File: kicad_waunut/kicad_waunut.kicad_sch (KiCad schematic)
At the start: 94 parts, among them J1 Conn_01x02_Pin, J2 Conn_01x06_Pin, Q1 NPN, Q2 NPN, Q3 NPN, Q4 NPN, Q5 NPN, Q6 NPN, Q7 NPN, Q8 NPN, U1 TSR1-2450E, U2 ATtiny861A-S

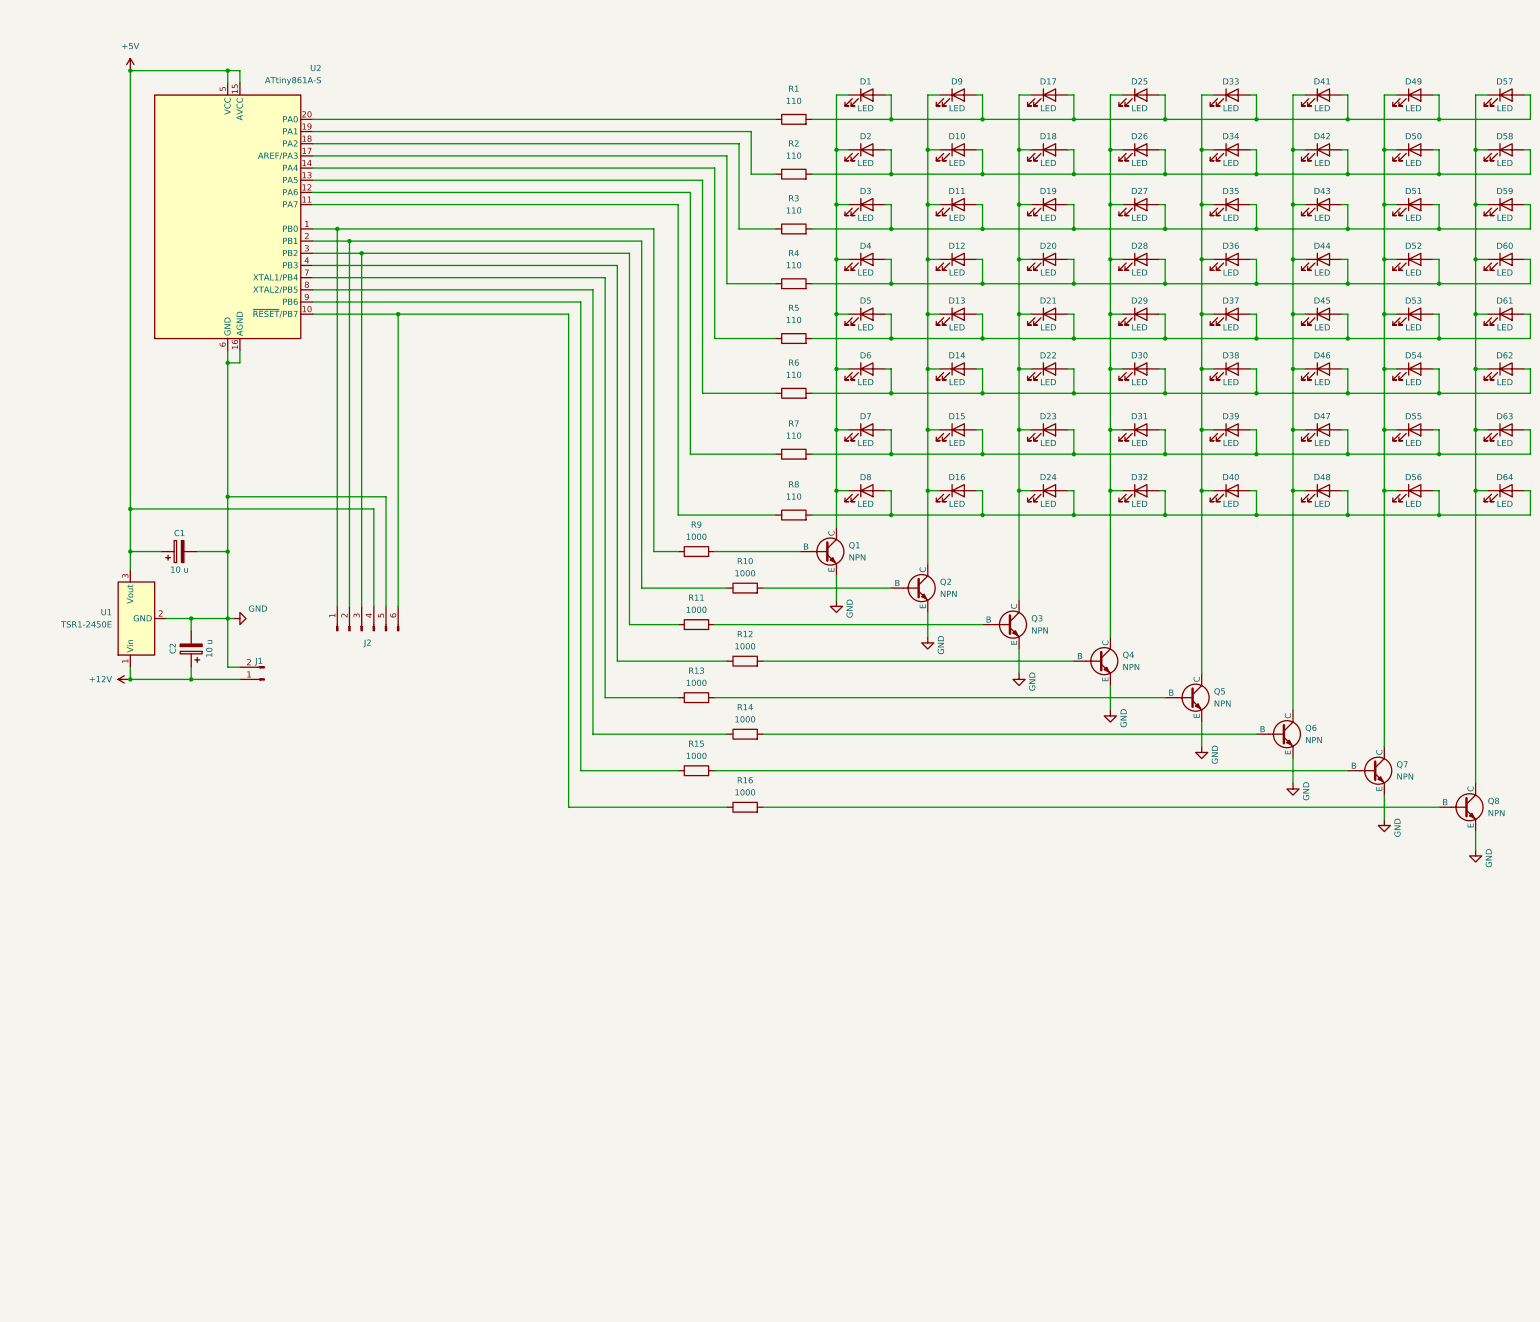
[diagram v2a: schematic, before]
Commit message: Kicad projekti tiedostoja siirrelty, selkä rev2 init ja waunujen skema muutosta.
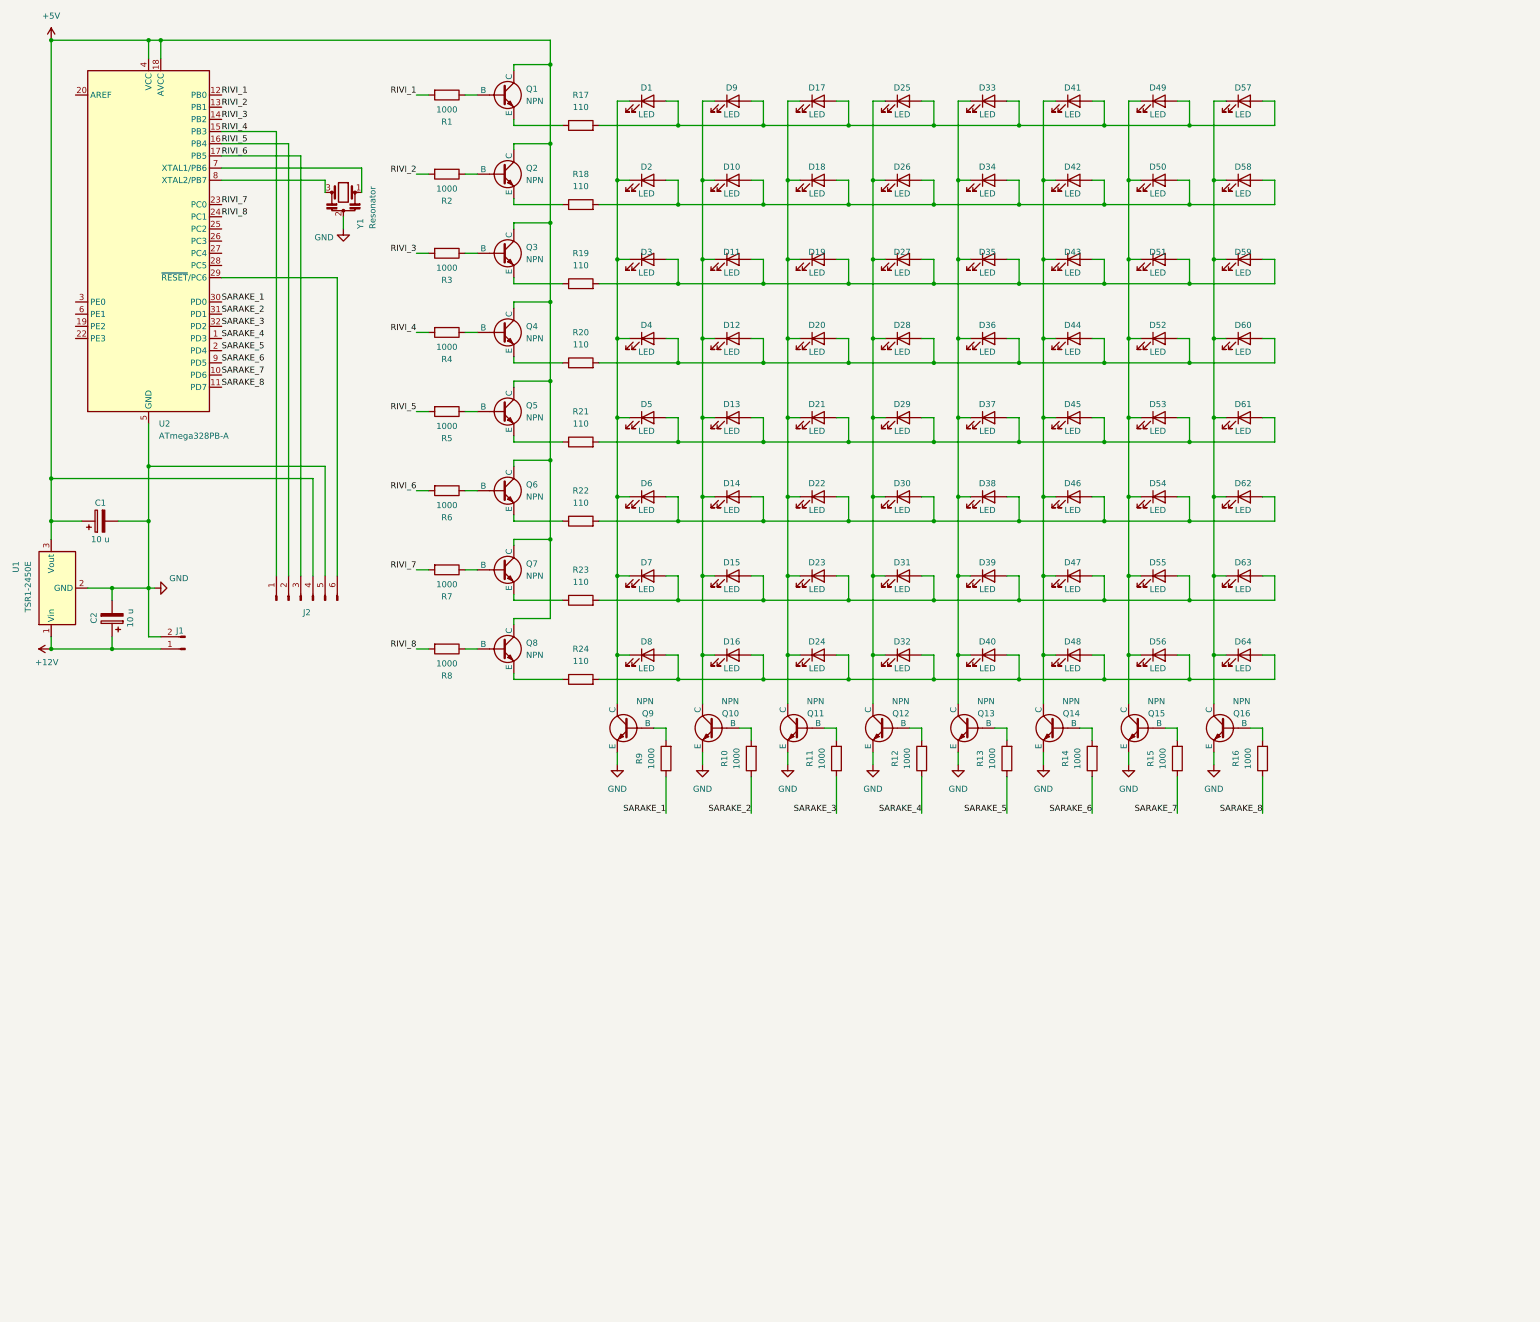
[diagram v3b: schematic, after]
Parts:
- removed U2: ATtiny861A-S, Package_SO:SOIC-20W_7.5x12.8mm_P1.27mm, symbol MCU_Microchip_ATtiny:ATtiny861A-S
- added Q10, Q11, Q12, Q13, Q14, Q15, Q16, Q9: NPN, Package_TO_SOT_SMD:SOT-23, symbol Simulation_SPICE:NPN
- added R1, R2, R3, R4, R5, R6, R7, R8: 1000, Resistor_SMD:R_1206_3216Metric_Pad1.30x1.75mm_HandSolder, symbol Device:R
- added U2: ATmega328PB-A, Package_QFP:TQFP-32_7x7mm_P0.8mm, symbol MCU_Microchip_ATmega:ATmega328PB-A
- added Y1: Resonator, symbol Device:Resonator
- renumbered R1 to R17, R2 to R18, R3 to R19, R4 to R20, R5 to R21, R6 to R22, R7 to R23, R8 to R24
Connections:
- net +5V: now also Q1.1 (C), Q2.1 (C), Q3.1 (C), Q4.1 (C), Q5.1 (C), Q6.1 (C), Q7.1 (C), Q8.1 (C), U2.18 (AVCC), U2.4 (VCC)
- net GND: now also Q10.3 (E), Q11.3 (E), Q12.3 (E), Q13.3 (E), Q14.3 (E), Q15.3 (E), Q16.3 (E), Q9.3 (E), U2.21 (GND), U2.5 (GND), Y1.2; no longer Q1.3 (E), Q2.3 (E), Q3.3 (E), Q4.3 (E), Q5.3 (E), Q6.3 (E), Q7.3 (E), Q8.3 (E)
- net at D17.1 (K), D18.1 (K), D19.1 (K)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: now also Q11.1 (C); no longer Q3.1 (C)
- net at R23.1: now also Q7.3 (E)
- net at D1.1 (K), D2.1 (K), D3.1 (K)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: now also Q9.1 (C); no longer Q1.1 (C)
- net at D57.1 (K), D58.1 (K), D59.1 (K)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: now also Q16.1 (C); no longer Q8.1 (C)
- net RIVI_4: now reaches J2.1 (Pin_1)
- net RIVI_4: now also R4.2, U2.15 (PB3); no longer R9.1
- net at R9.2: now also Q9.2 (B); no longer Q1.2 (B)
- net at D41.1 (K), D42.1 (K), D43.1 (K)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: now also Q14.1 (C); no longer Q6.1 (C)
- net at D10.1 (K), D11.1 (K), D12.1 (K)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: now also Q10.1 (C); no longer Q2.1 (C)
- net at D25.1 (K), D26.1 (K), D27.1 (K)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: now also Q12.1 (C); no longer Q4.1 (C)
- net at R20.1: now also Q4.3 (E)
- net RIVI_6: now reaches J2.3 (Pin_3)
- net RIVI_6: now also R6.2, U2.17 (PB5); no longer R11.1
- net at R11.2: now also Q11.2 (B); no longer Q3.2 (B)
- net at D49.1 (K), D50.1 (K), D51.1 (K)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: now also Q15.1 (C); no longer Q7.1 (C)
- net at D33.1 (K), D34.1 (K), D35.1 (K)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: now also Q13.1 (C); no longer Q5.1 (C)
- net SARAKE_4: now reaches R12.1
- net SARAKE_4: now also U2.1 (PD3)
- net at R12.2: now also Q12.2 (B); no longer Q4.2 (B)
- net RIVI_5: now reaches J2.2 (Pin_2)
- net RIVI_5: now also R5.2, U2.16 (PB4); no longer R10.1
- net at Q2.2 (B): now also R2.1; no longer R10.2
- net at R19.1: now also Q3.3 (E)
- net SARAKE_5: now reaches R13.1
- net SARAKE_5: now also U2.2 (PD4)
- net at Q5.2 (B): now also R5.1; no longer R13.2
- net at R16.2: now also Q16.2 (B); no longer Q8.2 (B)
- net at R14.2: now also Q14.2 (B); no longer Q6.2 (B)
- net at J2.6 (Pin_6): now also U2.29 (~{RESET}/PC6); no longer R16.1
- net at R17.1: now also Q1.3 (E)
- net at R21.1: now also Q5.3 (E)
- net at R22.1: now also Q6.3 (E)
- net at R24.1: now also Q8.3 (E)
- net SARAKE_6: now reaches R14.1
- net SARAKE_6: now also U2.9 (PD5)
- net at R18.1: now also Q2.3 (E)
- net SARAKE_7: now reaches R15.1
- net SARAKE_7: now also U2.10 (PD6)
- net at R15.2: now also Q15.2 (B); no longer Q7.2 (B)
- new net: Q6.2 (B), R6.1
- new net: Q10.2 (B), R10.2
- new net: Q13.2 (B), R13.2
- new net: U2.7 (XTAL1/PB6), Y1.1
- new net: U2.8 (XTAL2/PB7), Y1.3
- new net: Q7.2 (B), R7.1
- new net: Q8.2 (B), R8.1
- new net: Q1.2 (B), R1.1
- new net: Q3.2 (B), R3.1
- new net: Q4.2 (B), R4.1
- new net RIVI_1: R1.2, U2.12 (PB0)
- new net RIVI_2: R2.2, U2.13 (PB1)
- new net RIVI_3: R3.2, U2.14 (PB2)
- new net RIVI_7: R7.2, U2.23 (PC0)
- new net RIVI_8: R8.2, U2.24 (PC1)
- new net SARAKE_1: R9.1, U2.30 (PD0)
- new net SARAKE_2: R10.1, U2.31 (PD1)
- new net SARAKE_3: R11.1, U2.32 (PD2)
- new net SARAKE_8: R16.1, U2.11 (PD7)
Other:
- moved on the sheet: C1, C2, D1, D10, D11, D12, D13, D14, D15, D16, D17, D18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
